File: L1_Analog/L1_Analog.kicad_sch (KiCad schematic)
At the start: 36 parts, among them IC1 OPA380AIDR, IC2 TPS7A4901DGNR, J1 Conn_01x05_Socket, J2 Conn_01x05_Socket, U1 ADS1220xPW, U2 REF5045AD

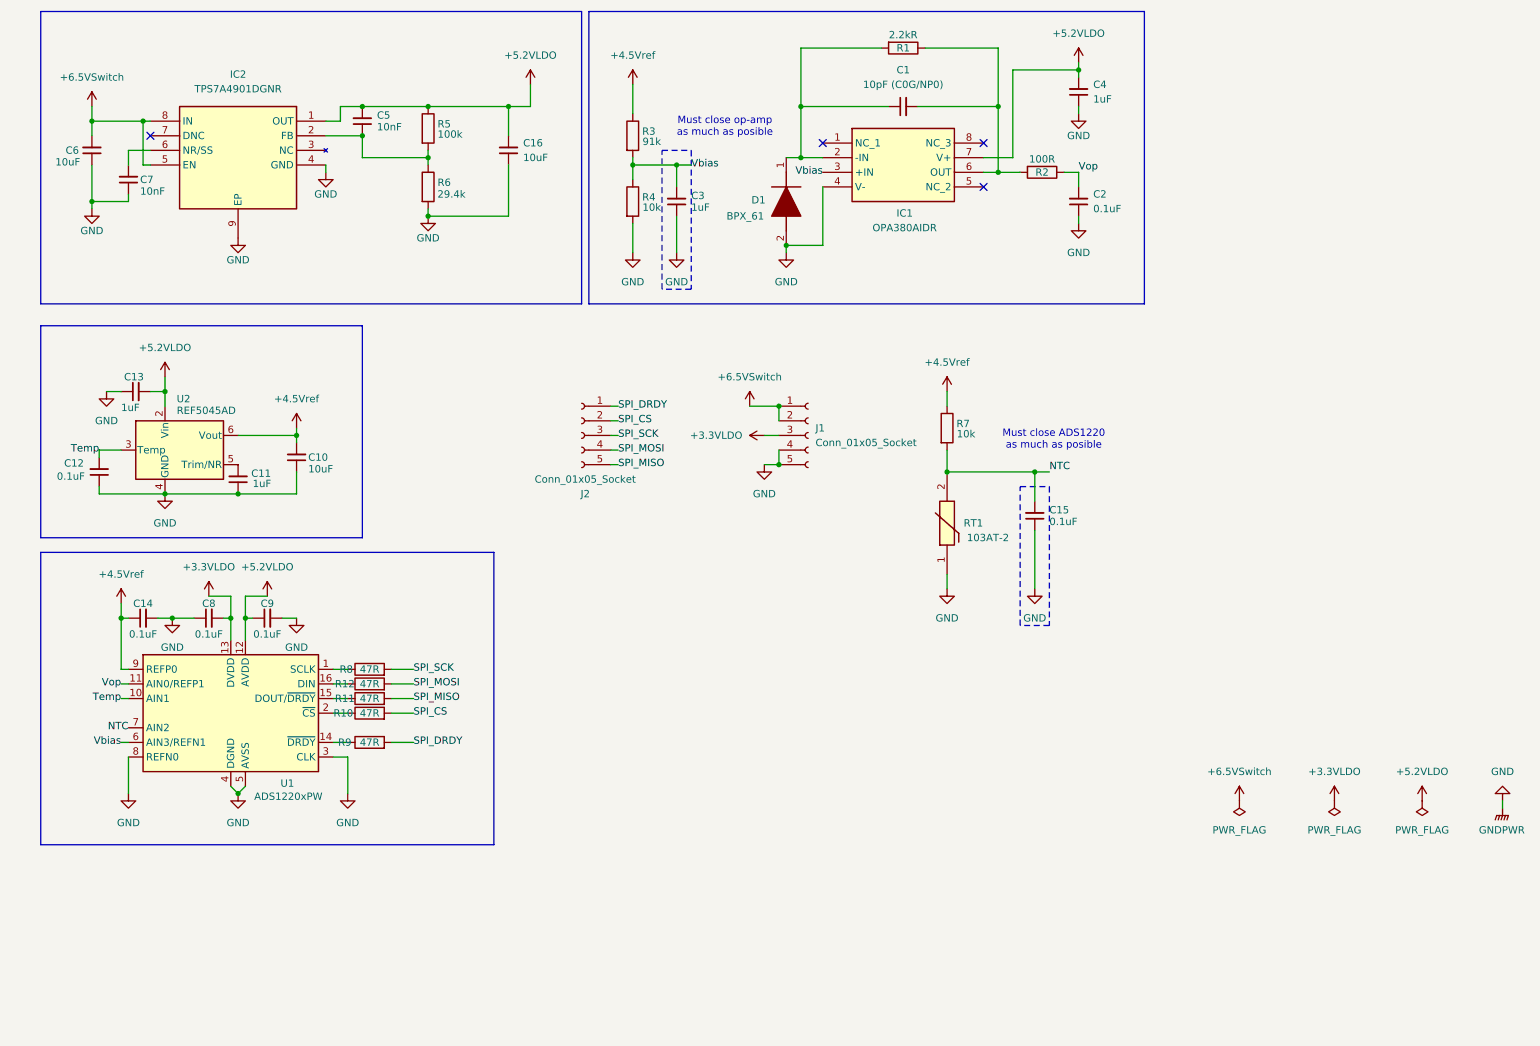
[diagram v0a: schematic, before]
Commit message: Document prototyping notes: ADS1220 differential MUX grouping and REF5045 C10/C11 capacitor requirements
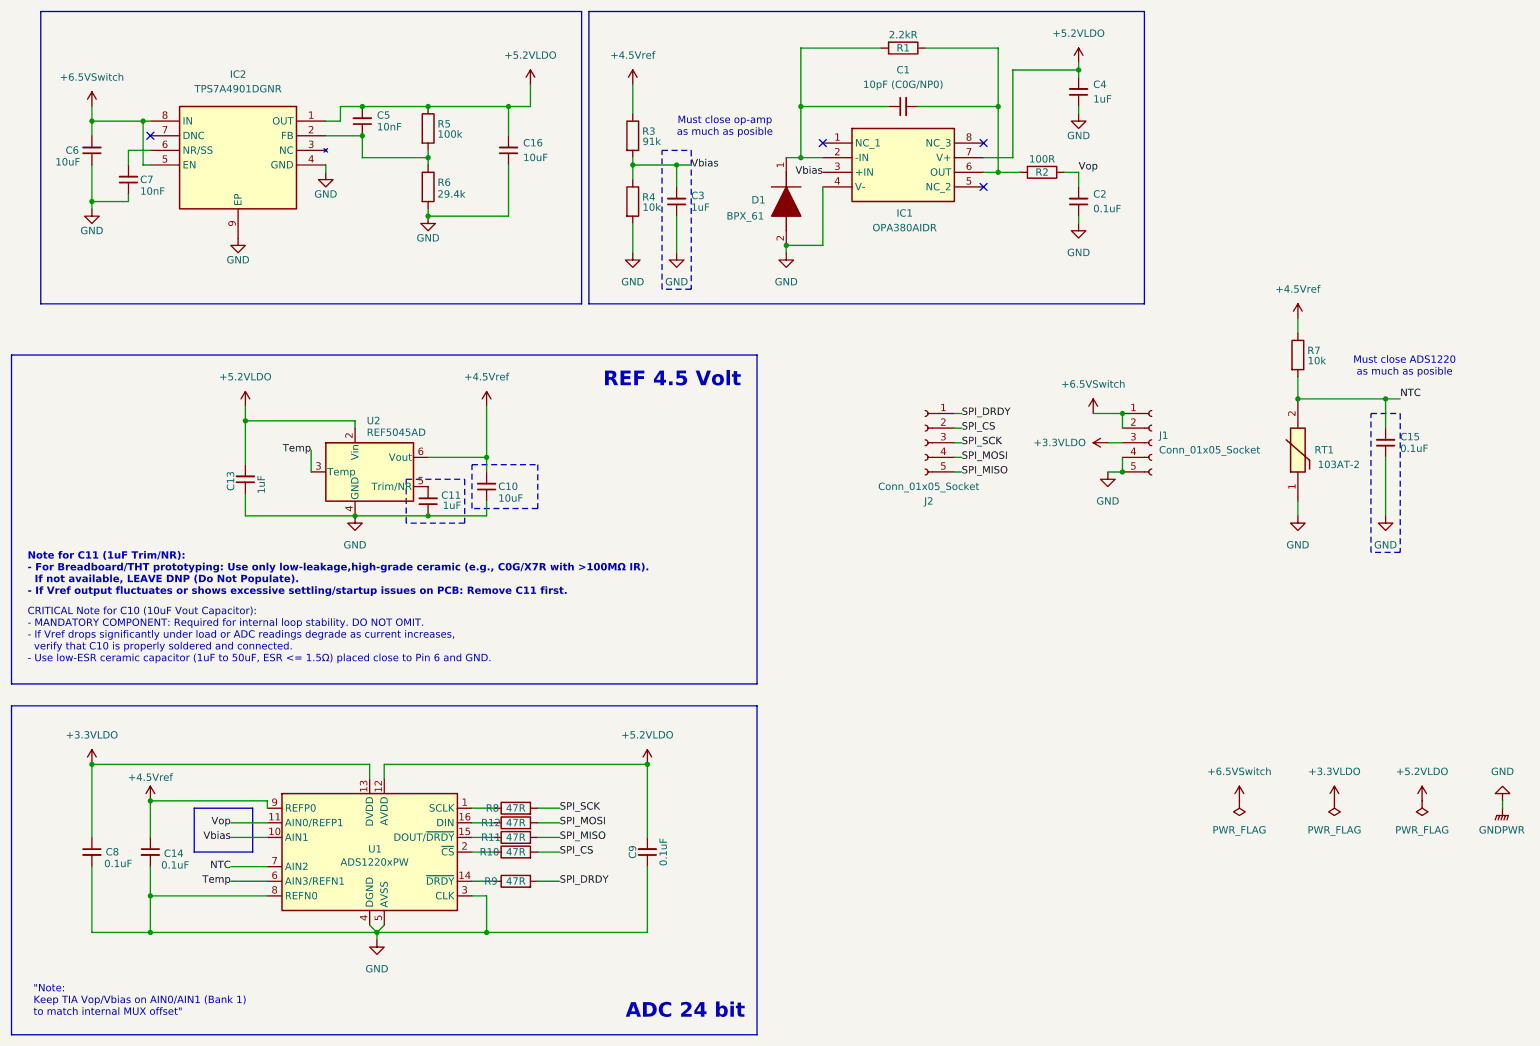
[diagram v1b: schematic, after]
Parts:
- removed C12: 0.1uF, Capacitor_SMD:C_0805_2012Metric, symbol Device:C_Small
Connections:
- net +3.3VLDO: now also C8.1; no longer C8.2
- net +5.2VLDO: now also C9.2; no longer C9.1
- net GND: now also C8.2, C9.1; no longer C8.1, C9.2
- net Temp: now also U1.6 (AIN3/REFN1); no longer U1.10 (AIN1)
- net Vbias: now also U1.10 (AIN1); no longer U1.6 (AIN3/REFN1)
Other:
- note added: ""Note: Keep TIA Vop/Vbias on AIN0/AIN1 (Bank 1) to match internal MUX offset""
- note added: "ADC 24 bit"
- note added: "CRITICAL Note for C10 (10uF Vout Capacitor): - MANDATORY COMPONENT: Required for internal loop stability. DO NOT OMIT. - If Vref drops significantly under load or ADC readings degrade as current increases, verify that C10 is properly soldered and connected. - Use low-ESR ceramic capacitor (1uF to 50uF, ESR <= 1.5Ω) placed close to Pin 6 and GND."
- note added: "Note for C11 (1uF Trim/NR): - For Breadboard/THT prototyping: Use only low-leakage,high-grade ceramic (e.g., C0G/X7R with >100MΩ IR). If not available, LEAVE DNP (Do Not Populate). - If Vref output fluctuates or shows excessive settling/startup issues on PCB: Remove C11 first."
- note added: "REF 4.5 Volt"
- moved on the sheet: C10, C11, C13, C14, C15, C8, C9, J1, J2, R10, R11, R12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
